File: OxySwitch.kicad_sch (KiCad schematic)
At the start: 5 parts, among them J101 Screw_Terminal_01x02, J102 Screw_Terminal_01x02, J103 Screw_Terminal_01x02, J104 Conn_ARM_JTAG_SWD_10

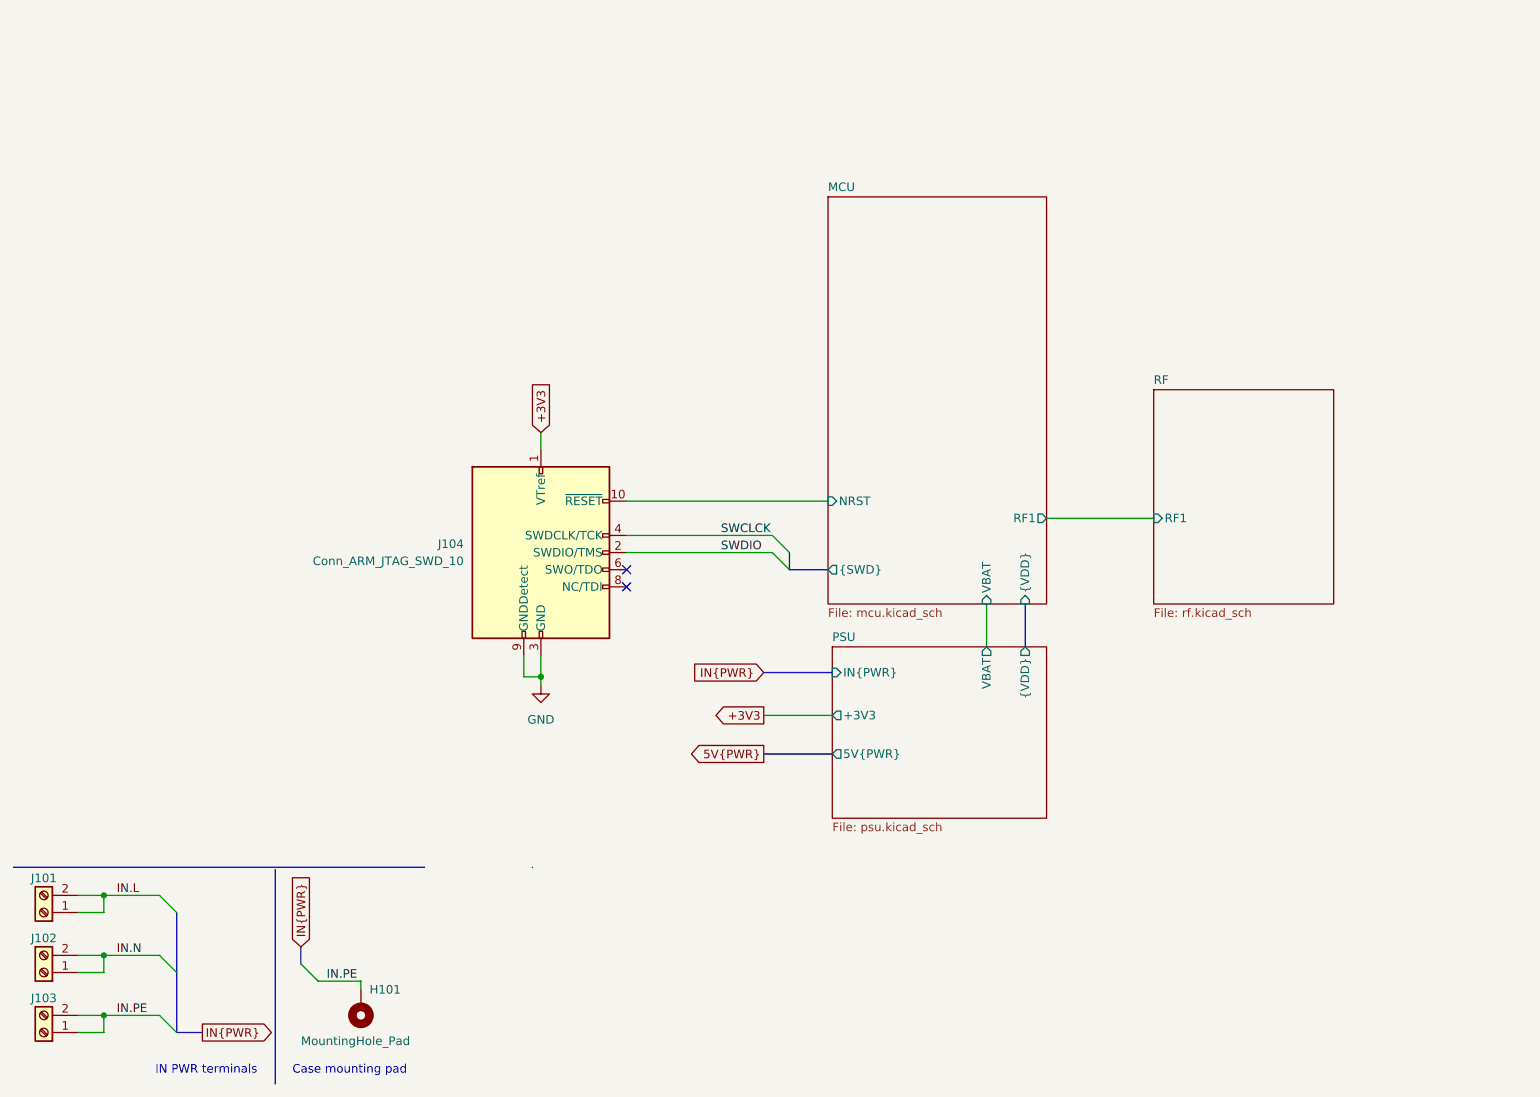
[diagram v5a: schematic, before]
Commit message: added zero detection
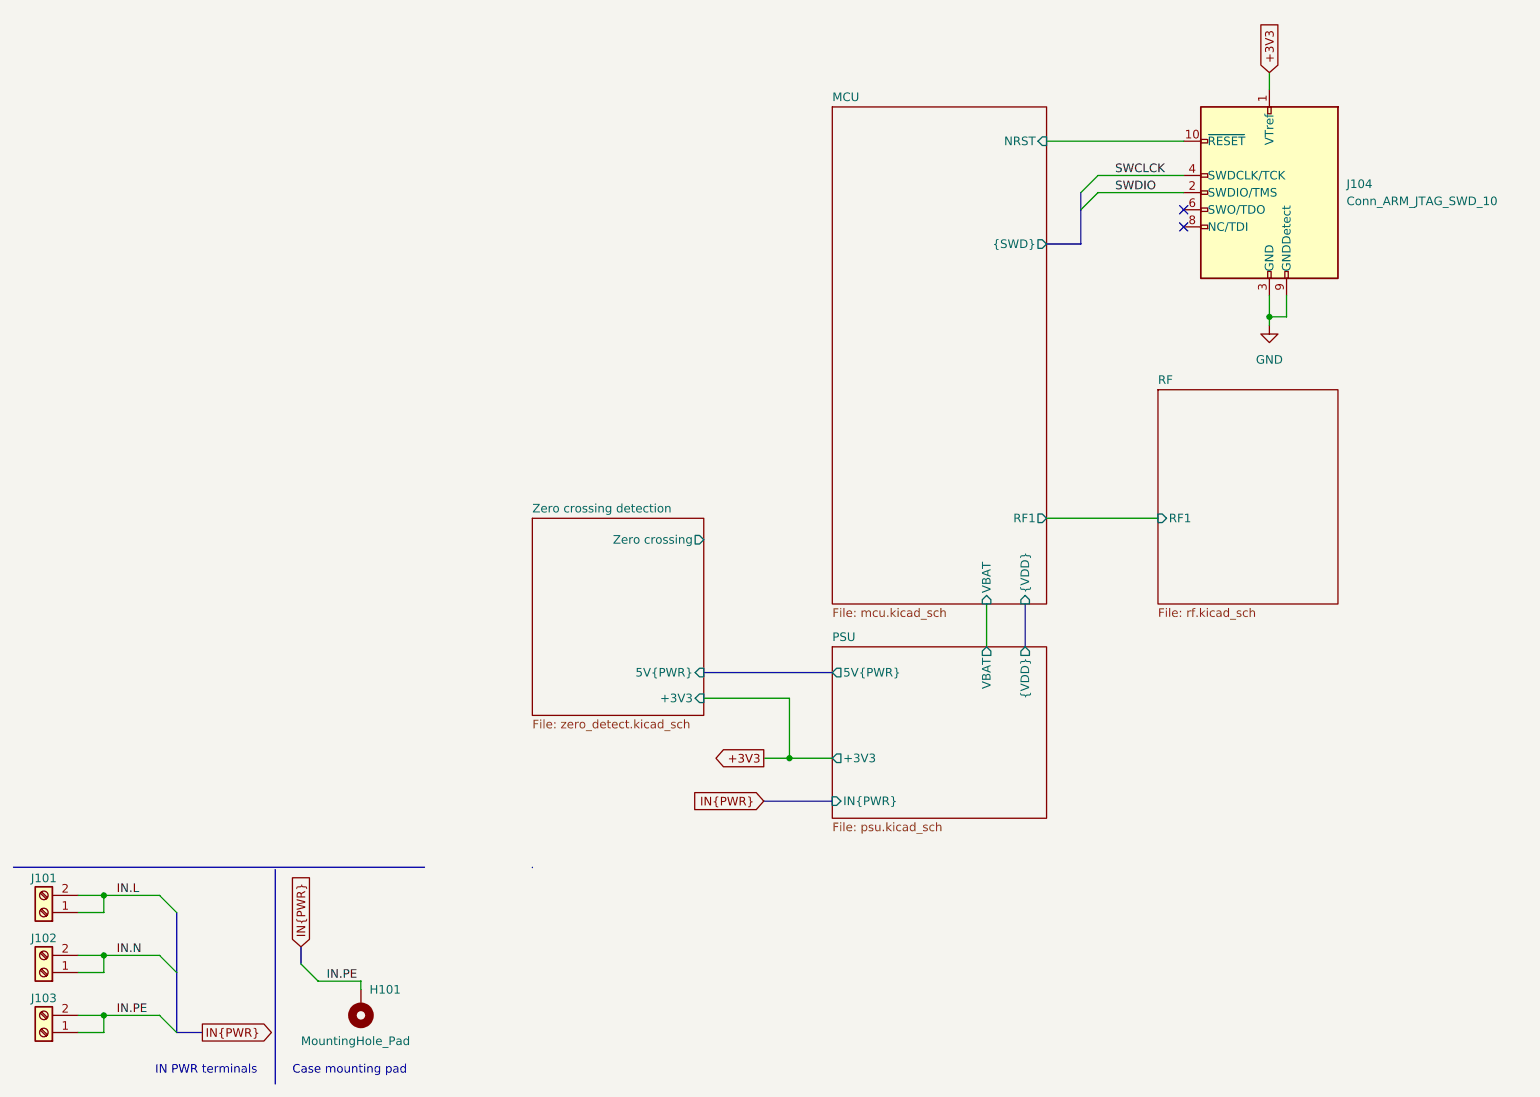
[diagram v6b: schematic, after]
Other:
- added sheet Zero crossing detection (zero_detect.kicad_sch)
- moved on the sheet: J104

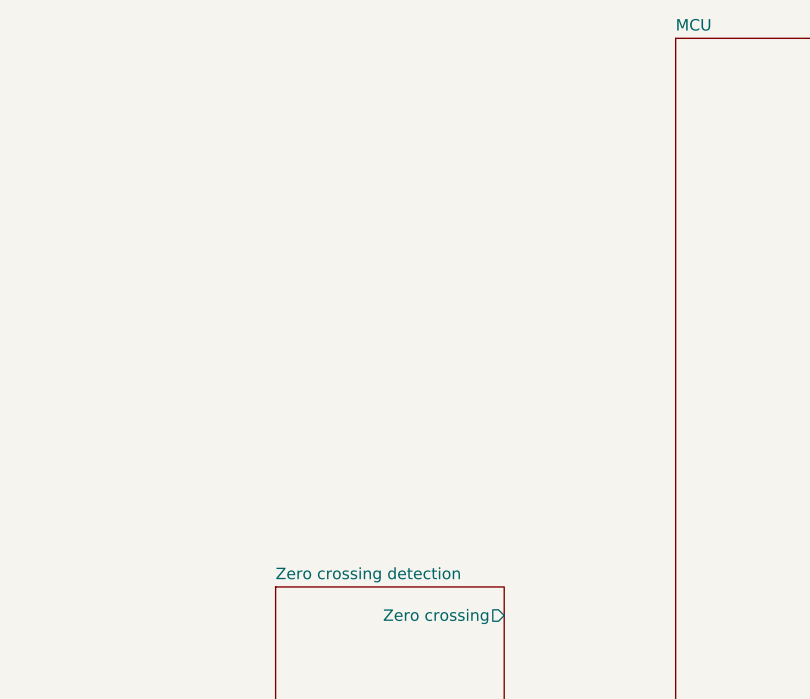
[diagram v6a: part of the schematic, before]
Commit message: Added Power circuit
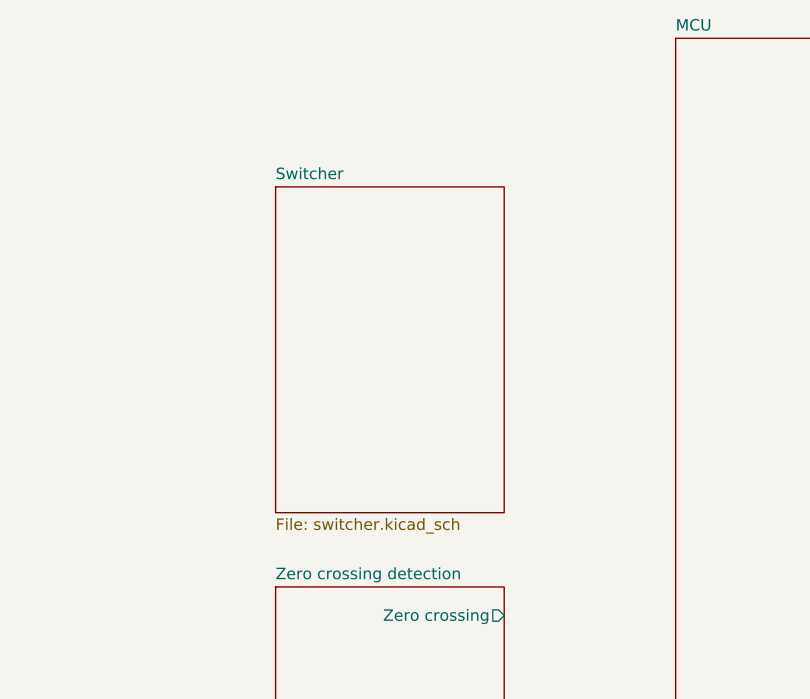
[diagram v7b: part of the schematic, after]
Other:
- added sheet Switcher (switcher.kicad_sch)
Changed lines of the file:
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@@
+    )
+  )
+  (sheet (at 88.9 69.85) (size 25.4 36.195) (fields_autoplaced)
+    (stroke (width 0.1524) (type solid) (color 0 0 0 0))
+    (fill (color 0 0 0 0.0000))
+    (property "Sheet name" "Switcher" (id 0) (at 88.9 69.1384 0)
+      (effects (font (size 1.27 1.27)) (justify left bottom))
+    )
+    (property "Sheet file" "switcher.kicad_sch" (id 1) (at 88.9 106.6296 0)
+      (effects (font (size 1.27 1.27)) (justify left top))
     )
   )
@@
     (path "/13cf60ac-65e2-4c08-a52d-012b34ab8e81/328173b0-1baf-4f2c-ac09-4ab7a43064f8" (page "4"))
     (path "/0168acc7-4fa4-4165-b008-de8faacbdcdc" (page "5"))
+    (path "/c48e78ef-f08a-426b-a4a4-dff90ce1874e" (page "7"))
     (path "/0e6e95a1-de17-47b1-9a9f-ed0cdb0b8e8a" (page "7"))
   )

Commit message: Finished basic version
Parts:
- added J104, J105, J106: Screw_Terminal_01x01, symbol Connector:Screw_Terminal_01x01
- renumbered J104 to J107
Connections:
- new net OUT.L: J104.1 (Pin_1)
- new net OUT.N: J105.1 (Pin_1)
- new net OUT.PE: J106.1 (Pin_1)
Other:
- sheet Switcher ports: added IN{PWR}, Main Control, OUT{PWR}; removed none
